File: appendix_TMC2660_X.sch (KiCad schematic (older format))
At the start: 60 parts, among them J601 B4B-XH-A, J602 B4B-XH-A, J603 B4B-XH-A, J604 B4B-XH-A, U601 TMC2660, U602 TMC2660, U603 TMC2660, U604 TMC2660

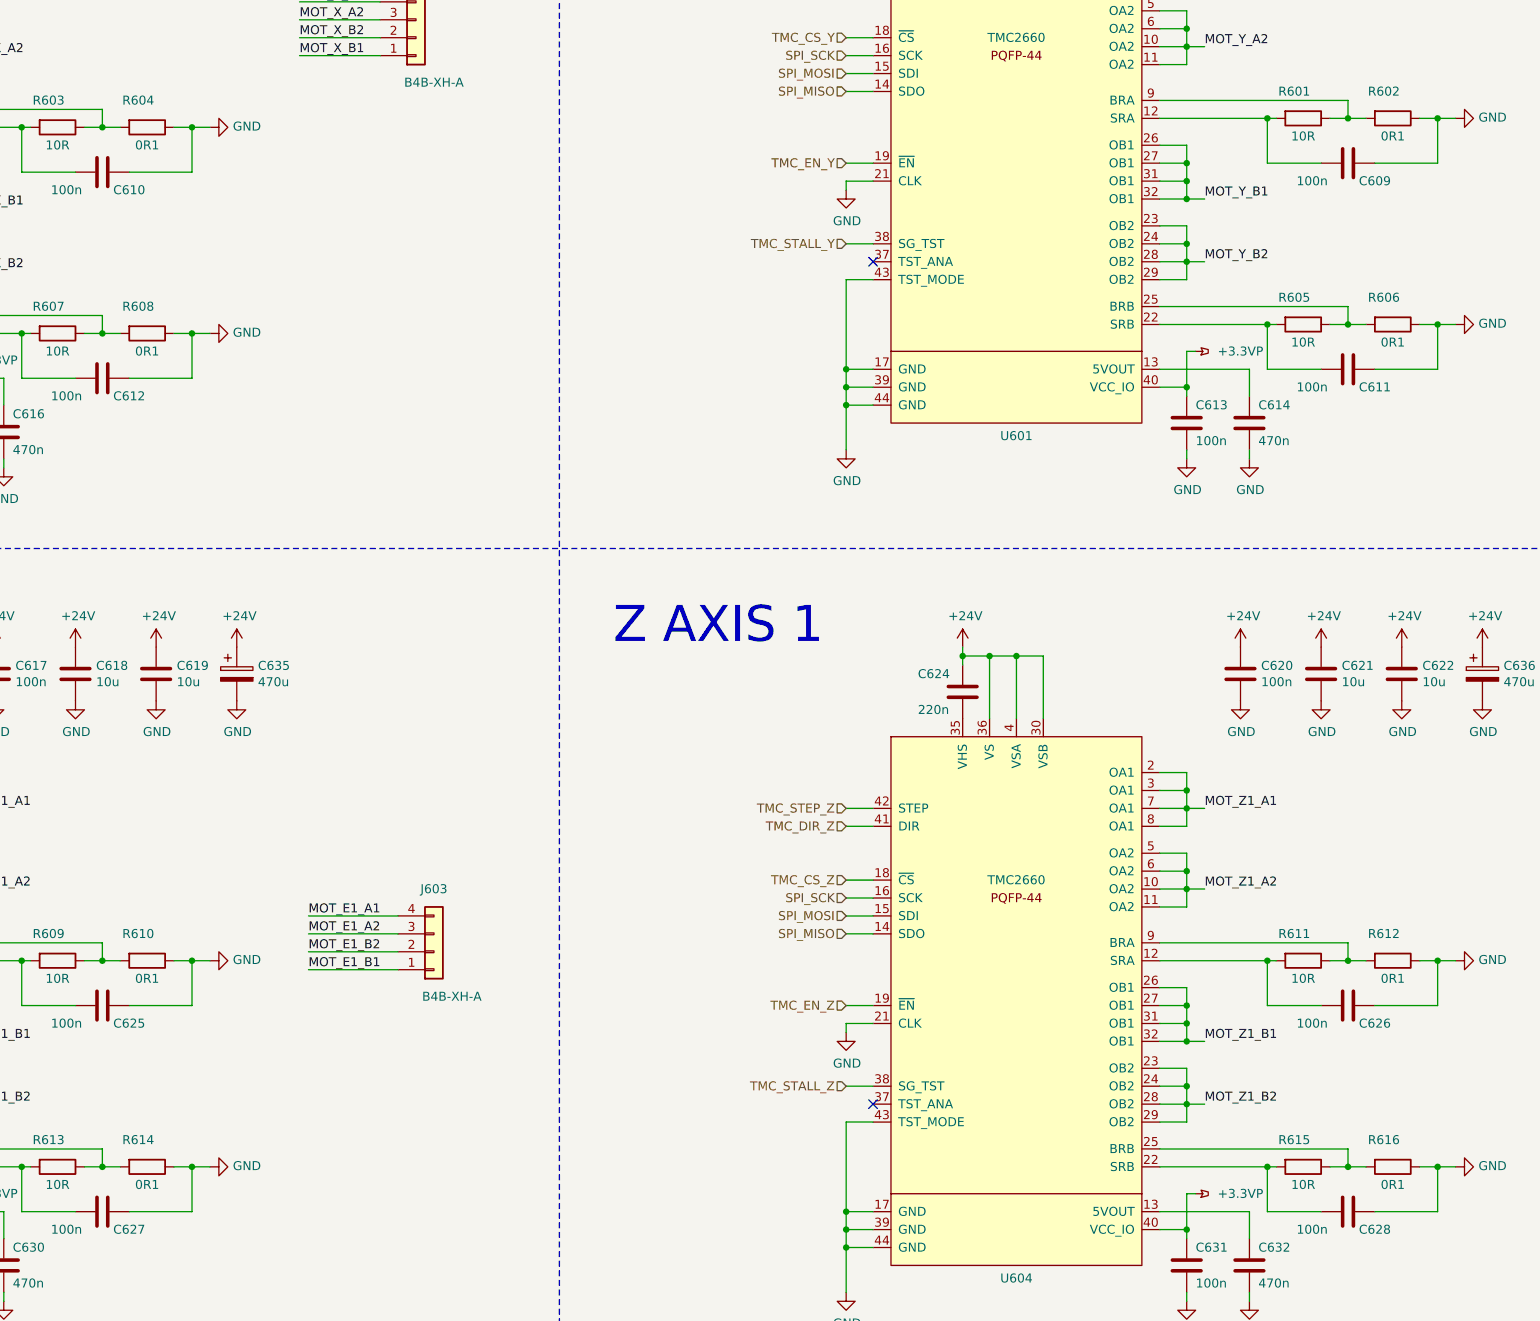
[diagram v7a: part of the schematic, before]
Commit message: added comments from comments branch corrected silk Servo2 added title to schematic pages
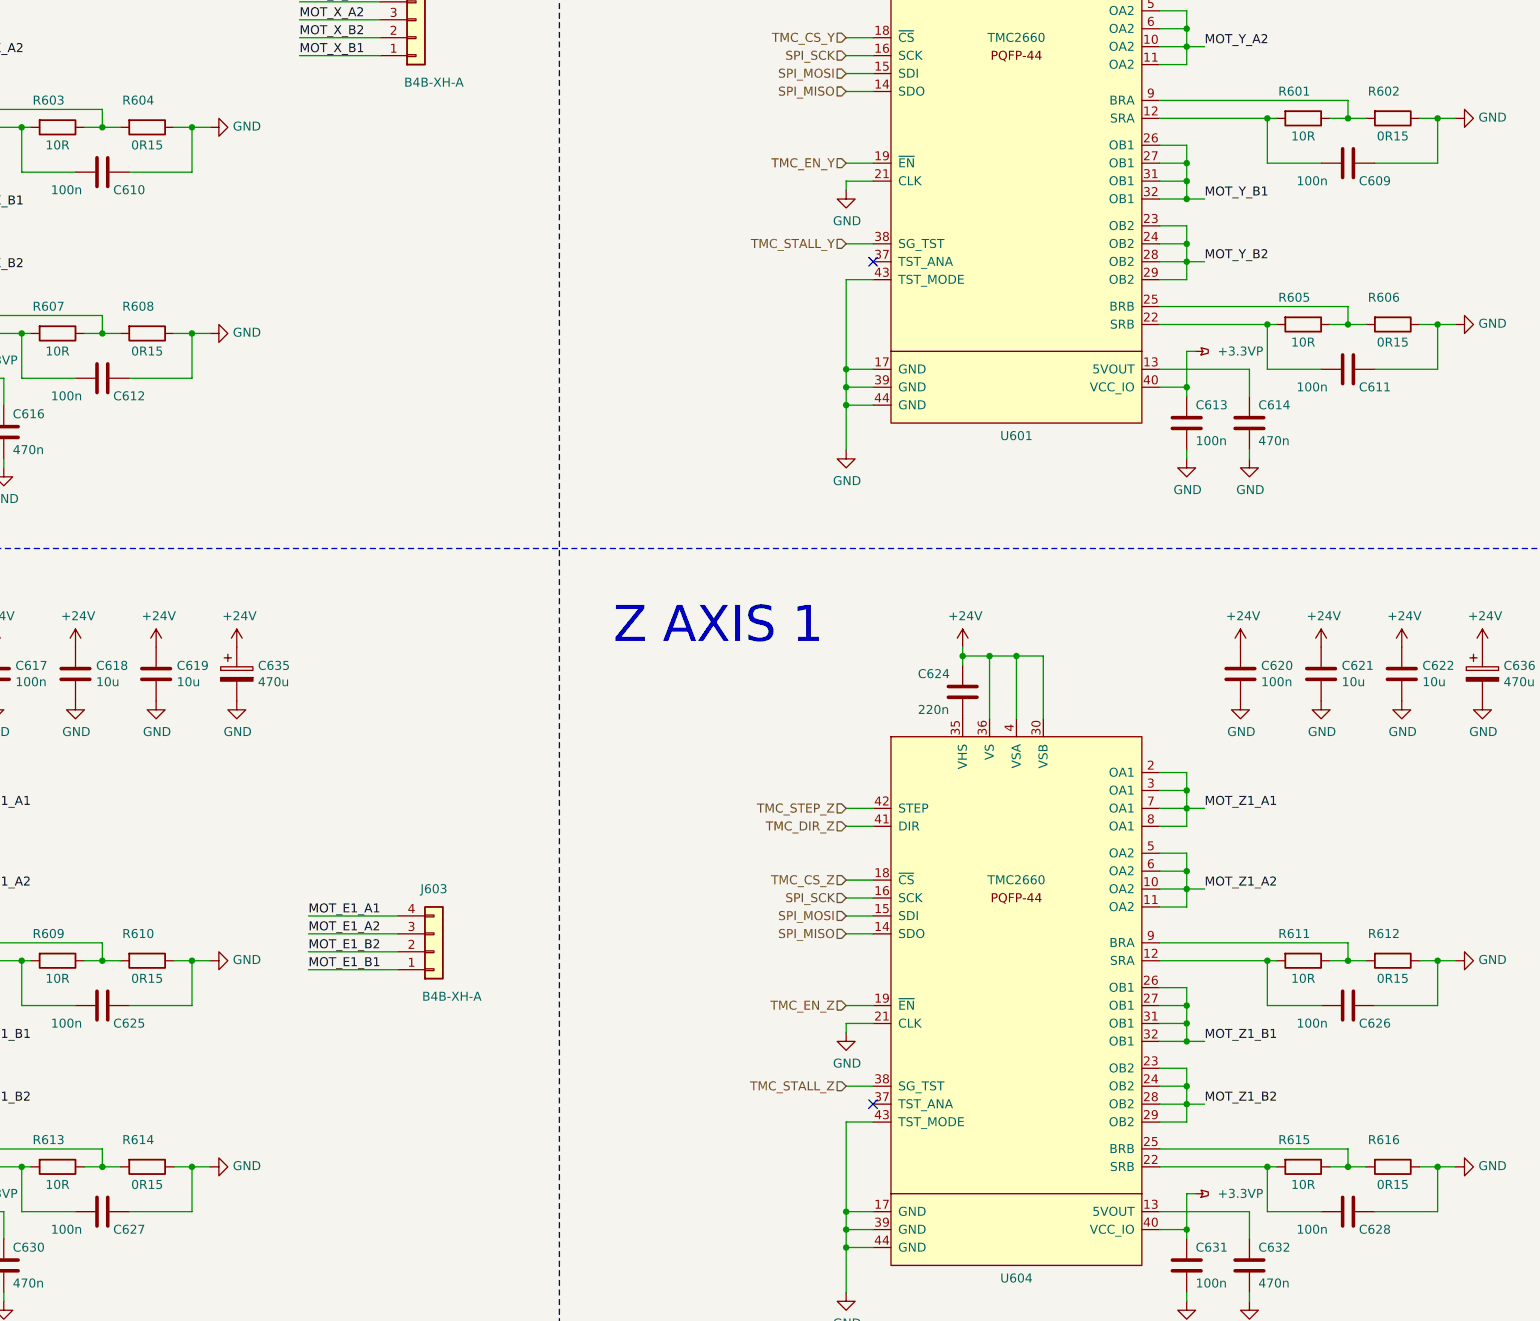
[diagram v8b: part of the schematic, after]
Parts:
- R602, R604, R606, R608, R610, R612, R614, R616: value 0R1 -> 0R15
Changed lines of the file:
@@
 Sheet 4 6
 Title "TMC2660 Stepper Drivers"
-Date ""
-Rev "1"
-Comp ""
+Date "2019-05-10"
+Rev "1.1"
+Comp "FHNW University of Applied Sciences"
 Comment1 "EIT Pro4 FS19 Team 8"
 Comment2 ""
@@
 P 5950 4000
 F 0 "R608" V 5800 3950 50  0000 C CNN
-F 1 "0R1" V 6050 4000 50  0000 C CNN
+F 1 "0R15" V 6050 4000 50  0000 C CNN
 F 2 "Resistors_SMD:R_1210" V 5880 4000 50  0001 C CNN
 F 3 "~" H 5950 4000 50  0001 C CNN
@@
 P 5950 2850
 F 0 "R604" V 5800 2800 50  0000 C CNN
-F 1 "0R1" V 6050 2850 50  0000 C CNN
+F 1 "0R15" V 6050 2850 50  0000 C CNN
 F 2 "Resistors_SMD:R_1210" V 5880 2850 50  0001 C CNN
 F 3 "~" H 5950 2850 50  0001 C CNN
@@
 P 12900 3950
 F 0 "R606" V 12750 3900 50  0000 C CNN
-F 1 "0R1" V 13000 3950 50  0000 C CNN
+F 1 "0R15" V 13000 3950 50  0000 C CNN
 F 2 "Resistors_SMD:R_1210" V 12830 3950 50  0001 C CNN
 F 3 "~" H 12900 3950 50  0001 C CNN
@@
 P 12900 2800
 F 0 "R602" V 12750 2750 50  0000 C CNN
-F 1 "0R1" V 13000 2800 50  0000 C CNN
+F 1 "0R15" V 13000 2800 50  0000 C CNN
 F 2 "Resistors_SMD:R_1210" V 12830 2800 50  0001 C CNN
 F 3 "~" H 12900 2800 50  0001 C CNN
@@
 P 12900 8650
 F 0 "R616" V 12750 8600 50  0000 C CNN
-F 1 "0R1" V 13000 8650 50  0000 C CNN
+F 1 "0R15" V 13000 8650 50  0000 C CNN
 F 2 "Resistors_SMD:R_1210" V 12830 8650 50  0001 C CNN
 F 3 "~" H 12900 8650 50  0001 C CNN
@@
 P 12900 7500
 F 0 "R612" V 12750 7450 50  0000 C CNN
-F 1 "0R1" V 13000 7500 50  0000 C CNN
+F 1 "0R15" V 13000 7500 50  0000 C CNN
 F 2 "Resistors_SMD:R_1210" V 12830 7500 50  0001 C CNN
 F 3 "~" H 12900 7500 50  0001 C CNN
@@
 P 5950 8650
 F 0 "R614" V 5800 8600 50  0000 C CNN
-F 1 "0R1" V 6050 8650 50  0000 C CNN
+F 1 "0R15" V 6050 8650 50  0000 C CNN
 F 2 "Resistors_SMD:R_1210" V 5880 8650 50  0001 C CNN
 F 3 "~" H 5950 8650 50  0001 C CNN
@@
 P 5950 7500
 F 0 "R610" V 5800 7450 50  0000 C CNN
-F 1 "0R1" V 6050 7500 50  0000 C CNN
+F 1 "0R15" V 6050 7500 50  0000 C CNN
 F 2 "Resistors_SMD:R_1210" V 5880 7500 50  0001 C CNN
 F 3 "~" H 5950 7500 50  0001 C CNN
